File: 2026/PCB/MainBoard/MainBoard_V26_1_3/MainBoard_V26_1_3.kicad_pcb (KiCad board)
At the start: 2 copper layers, 100 x 65 mm, 94 parts, among them J1 Raspberry_Pi_2_3, J15 TFT3, J16 CAN_CON, J2 fan, J3 MOLEX, J5 Conn_01x05_Socket, J6 Debug, Q1 Q_NMOS_GSD, Q2 Q_NMOS_GSD, SW1 SW_MEC_5E, SW2 Ras_1, SW3 Ras_2, SW4 SW_Wuerth_450301014042, SW5 SW_MEC_5E, SW6 SW_MEC_5E, U1 STM32F446RETx, U10 MPU9250, U2 LMR51460FSQDRRRQ1, U3 MOUDLE-SEEEDUINO-XIAO, U5 MCP1703AT-3302E/CB, U6 BNO055, U7 LTC4451AV-TRPBF, U8 MAX3051, Y1 CSTNE16M0V530000R0

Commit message: 回路修正、PCB大枠決定
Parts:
- removed R9: 2.2k, Resistor_SMD:R_0603_1608Metric_Pad0.98x0.95mm_HandSolder
- removed SW4: SW_Wuerth_450301014042, 0_Library:slideSW
- removed SW5, SW6: SW_MEC_5E, 0_Library:SW_SKRPACE010
- removed U10: MPU9250, Connector_PinHeader_2.54mm:PinHeader_1x10_P2.54mm_Vertical
- added C26: 0.1u, Capacitor_SMD:C_0603_1608Metric_Pad1.08x0.95mm_HandSolder, F.Cu at (204.3, 33.6)
- added C27: 0.1u, Capacitor_SMD:C_0603_1608Metric_Pad1.08x0.95mm_HandSolder, F.Cu at (204.3, 36.1)
- added C28: 0.1u, Capacitor_SMD:C_0603_1608Metric_Pad1.08x0.95mm_HandSolder, F.Cu at (204.3, 38.6)
- added R1: 100k, Resistor_SMD:R_0603_1608Metric_Pad0.98x0.95mm_HandSolder, F.Cu at (204.3, 41.1)
- added U9: LTC4451AV-TRPBF, 0_Library:05-08-1683_ADI, F.Cu at (208.5, 39.7)
- R10: value 4.7k -> 100k
- R11: value 1k -> 10k
- R8: value 2.2k -> 10k
- SW1: moved to F.Cu
- U3: moved to B.Cu
- U6: value BNO055 -> LSM6DSO32XTR; footprint Connector_PinHeader_2.54mm:PinHeader_1x04_P2.54mm_Vertical -> 0_Library:LGA_O32XTR_STM-M; moved to F.Cu
- moved ROTSW1 85.8 mm to (251.6, 68.5), turned to 90 degrees
- moved G*** 78.3 mm to (138.7, 63.7)
- moved SW3 67.5 mm to (248.7, 61.2), turned to -90 degrees
- moved R8 64.3 mm to (204.3, 43.6), turned to 0 degrees
- moved U3 62.9 mm to (252.1, 124.3)
- moved SW1 61.1 mm to (232.2, 61.7), turned to 0 degrees
- moved SW2 51.1 mm to (241.2, 61.2), turned to -90 degrees
- moved U6 44.6 mm to (214.4, 84.5)
- moved G*** 15.4 mm to (188.7, 46.4)
- moved C24 5.20 mm to (188.2, 81.4), turned to 90 degrees
- moved D11 4.59 mm to (259.2, 108.0)
- moved D14 4.59 mm to (259.2, 105.0)
- moved D3 4.59 mm to (259.2, 106.5)
- moved R16 4.59 mm to (259.2, 108.0)
- moved R19 4.59 mm to (259.2, 105.0)
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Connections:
- C18 pad 1: +5V -> 5V_For3.3V
- D3 pad 2: 5V_Rock -> +5V
- J1 pad 26: unconnected-(J1-~{CE1}/GPIO7-Pad26) -> ESTOP
- R8 pad 1: I2C_SDA -> ESTOP
- U1 pad 24: SPI1.CS -> unconnected-(U1-PC4-Pad24)
- U1 pad 28: SPI2.CS -> unconnected-(U1-PB2-Pad28)
- U1 pad 33: LED1 -> SPI2.CS
- U1 pad 39: imu.reset -> unconnected-(U1-PC8-Pad39)
- U1 pad 50: unconnected-(U1-PA15-Pad50) -> SPI1.CS
- U1 pad 57: discharge -> unconnected-(U1-PB5-Pad57)
- U1 pad 58: I2C_SCL -> unconnected-(U1-PB6-Pad58)
- U1 pad 59: I2C_SDA -> unconnected-(U1-PB7-Pad59)
- U1 pad 60: Net-(SW4-B) -> unconnected-(U1-BOOT0-Pad60)
- U1 pad 61: unconnected-(U1-PB8-Pad61) -> LED1
- U1 pad 8: unconnected-(U1-PC0-Pad8) -> ESTOP
- U5 pad 3: +5V -> 5V_For3.3V
- U6 pad 1: +3.3V -> SPI1.MISO
- U6 pad 3: I2C_SDA -> GND
- U6 pad 4: I2C_SCL -> unconnected-(U6-INT1-Pad4)
- U7 pad 1: +5V -> unconnected-(U7-VCC-Pad1)
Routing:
- net +3.3V: track 314.4 -> 0.00 mm, vias 9 -> 0
- net 5V_Rock: track 131.9 -> 0.00 mm, vias 19 -> 0
- net +5V: track 113.1 -> 0.00 mm, vias 4 -> 0
- net LED_RAS2: track 113.1 -> 0.00 mm, vias 1 -> 0
- net LED_RAS1: track 110.6 -> 0.00 mm, vias 1 -> 0
- net SPI2.CS: track 94.1 -> 0.00 mm, vias 2 -> 0
- net SPI2.CLK: track 80.8 -> 0.00 mm, vias 2 -> 0
- net UI_Audio: track 78.5 -> 0.00 mm, vias 1 -> 0
- net NRST: track 69.0 -> 0.00 mm, vias 5 -> 0
- net LED_CS: track 64.6 -> 0.00 mm, vias 1 -> 0
- net SPI2.MOSI: track 63.6 -> 0.00 mm
- net SPI1.CLK: track 60.7 -> 0.00 mm, vias 1 -> 0
- net SPI2.MISO: track 60.5 -> 0.00 mm
- net BATTERY_MEASURE: track 59.5 -> 0.00 mm, vias 2 -> 0
- net MD3_TX: track 57.7 -> 0.00 mm, vias 2 -> 0
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- removed copper zone on B.Cu, net +24V
- removed copper zone on B.Cu, net Net-(C15-Pad2)
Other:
- board text removed: "BOOT-ON/OFF"
- board text removed: "Discharge"
- board text removed: "IMU"

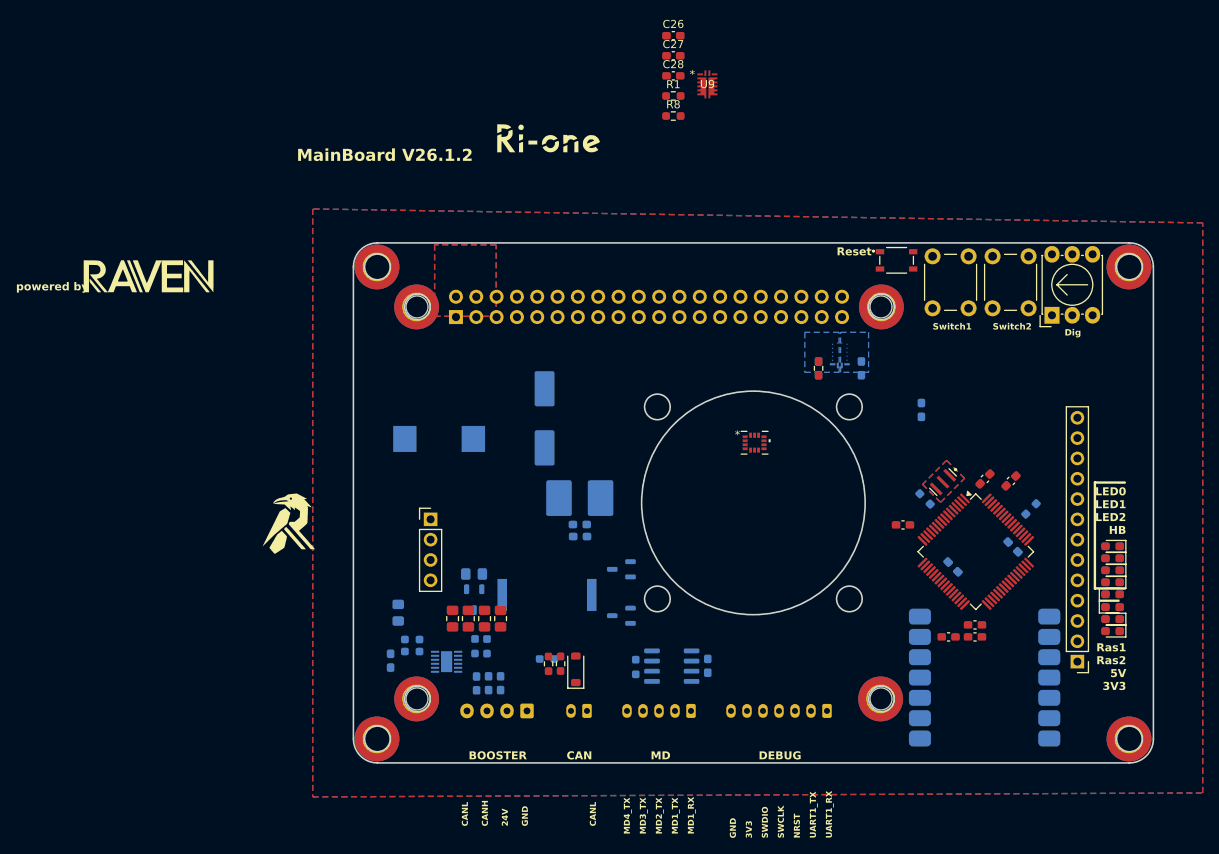
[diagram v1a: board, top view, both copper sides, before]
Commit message: 基板外形、ESTOP変更、配置決定
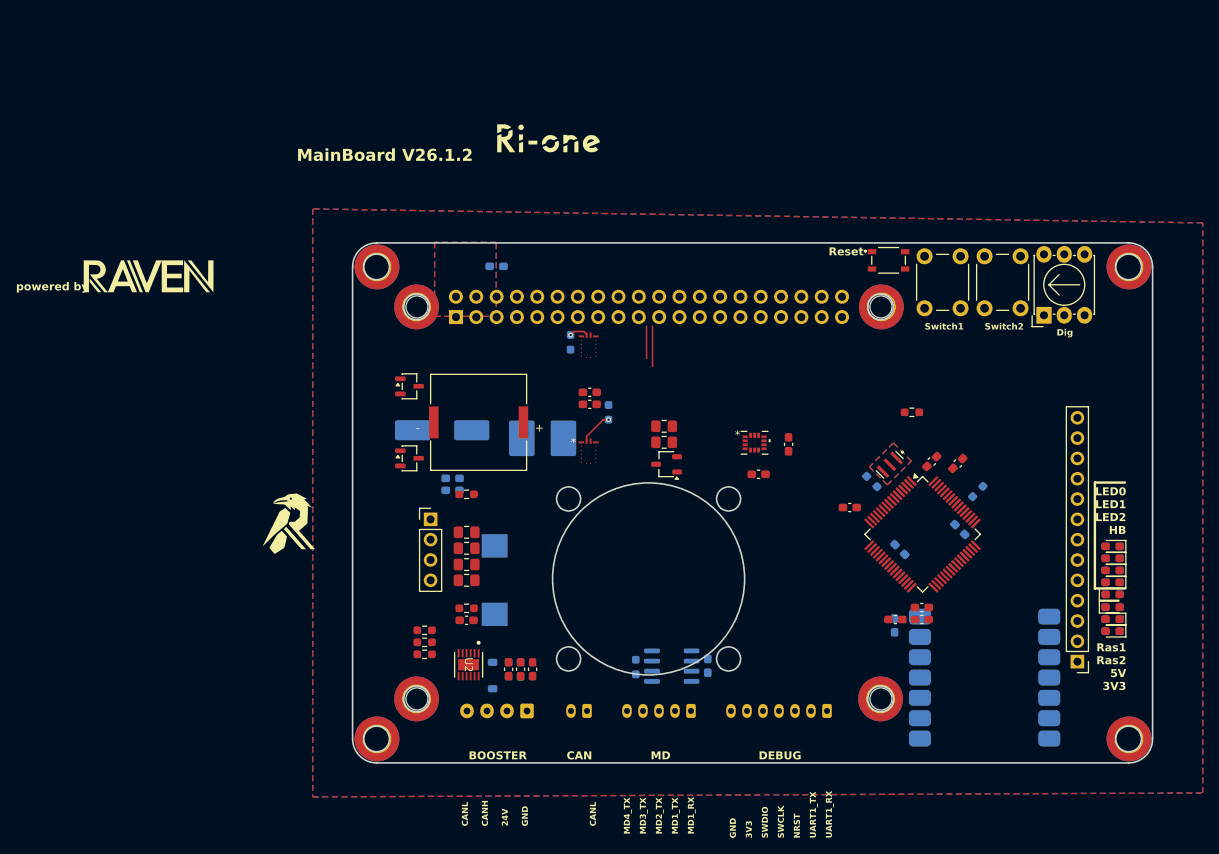
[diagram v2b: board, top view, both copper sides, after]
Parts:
- C11, C13, C15, C17, C18, C19, C25, LS1, Q1, Q2, R2, R21, R3, R4, R7, U2, U5, U7: moved to F.Cu
- D6, R1, R10, R11, R17: moved to B.Cu
- moved C27 53.4 mm to (214.9, 88.4), turned to 180 degrees
- moved U9 48.3 mm to (193.7, 85.7)
- moved C28 48.3 mm to (218.7, 84.7), turned to -90 degrees
- moved R8 47.5 mm to (234.1, 80.7)
- moved C23 47.3 mm to (182.2, 62.4), turned to 0 degrees
- moved C26 47.2 mm to (193.9, 79.7)
- moved R1 40.4 mm to (196.2, 80.7), turned to 90 degrees
- moved C18 39.5 mm to (203.1, 84.4), turned to 0 degrees
- moved Q1 35.0 mm to (171.3, 77.4), turned to 0 degrees
- moved Q2 33.0 mm to (171.3, 86.4), turned to 0 degrees
- moved U7 31.4 mm to (193.7, 72.4)
- moved R17 31.2 mm to (191.4, 71.9), turned to -90 degrees
- moved C17 30.1 mm to (203.1, 82.4), turned to 0 degrees
- moved U5 29.4 mm to (203.4, 87.2), turned to 180 degrees
- moved C25 28.8 mm to (193.9, 78.2), turned to 0 degrees
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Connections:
- J1 pad 26: ESTOP -> unconnected-(J1-~{CE1}/GPIO7-Pad26)
- J1 pad 37: unconnected-(J1-GPIO26-Pad37) -> ESTOP
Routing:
- net Net-(U9-SHDN#): track 0.00 -> 4.21 mm, vias 0 -> 1
- net Net-(U7-SHDN#): track 0.00 -> 2.47 mm, vias 0 -> 1
- removed copper zone on B.Cu, net +5V
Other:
- outline, holes or cut-outs redrawn

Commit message: 途中保存
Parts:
- R8: moved to B.Cu
- moved R5 10.2 mm to (229.7, 79.2), turned to -135 degrees
- moved R8 6.29 mm to (228.4, 77.9), turned to 45 degrees
- moved C1 6.05 mm to (232.8, 100.6)
- moved C2 6.05 mm to (237.3, 80.8)
- moved C4 6.05 mm to (236.1, 99.1)
- moved C5 6.05 mm to (240.8, 89.3)
- moved C6 6.05 mm to (240.6, 81.1)
- moved C7 6.05 mm to (227.1, 86.6)
- moved C8 6.05 mm to (236.1, 100.6)
- moved R1 6.05 mm to (243.1, 84.6)
- moved U1 6.05 mm to (236.2, 89.9)
- moved Y1 6.05 mm to (232.1, 81.2)
- moved C3 4.16 mm to (229.2, 95.4)
- moved R7 0.50 mm to (178.4, 90.4)
- moved C25 0.15 mm to (193.7, 78.2)
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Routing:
- net +3.3V: track 0.00 -> 115.9 mm, vias 0 -> 1
- net SPI2.CLK: track 0.00 -> 40.6 mm, vias 0 -> 1
- net SPI2.CS: track 0.00 -> 39.6 mm, vias 0 -> 1
- net SPI2.MOSI: track 0.00 -> 39.2 mm, vias 0 -> 1
- net SPI2.MISO: track 0.00 -> 36.5 mm, vias 0 -> 1
- net NRST: track 0.00 -> 25.9 mm, vias 0 -> 3
- net LED_CS: track 0.00 -> 25.8 mm, vias 0 -> 1
- net ESTOP: track 0.00 -> 20.9 mm, vias 0 -> 1
- net Net-(Q1-D): track 0.00 -> 17.8 mm
- net +5V: track 0.00 -> 14.9 mm, vias 0 -> 24
- net D/C: track 0.00 -> 10.8 mm
- net Net-(U2-PG): track 0.00 -> 6.44 mm
- net Net-(U2-FB): track 0.00 -> 6.07 mm
- net Net-(U1-PH0): track 0.00 -> 5.13 mm
- net Net-(U2-RT): track 0.00 -> 5.03 mm
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- added copper zone on F.Cu, net +24V
- added copper zone on B.Cu, net +5V
- added copper zone on F.Cu, net +5V
- added copper zone on F.Cu, net 5V_For3.3V
- added copper zone on B.Cu, net Net-(C15-Pad2)
- added copper zone on F.Cu, net Net-(C15-Pad2)

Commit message: 途中保存2
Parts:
- C16, R20, U3, U8: moved to F.Cu
- moved D13 80.7 mm to (188.8, 63.9)
- moved R18 80.7 mm to (188.8, 63.9)
- moved D14 77.6 mm to (193.3, 63.9)
- moved R19 77.6 mm to (193.3, 63.9)
- moved G*** 24.6 mm to (212.7, 51.7)
- moved R20 20.7 mm to (220.3, 111.9), turned to 180 degrees
- moved U3 17.8 mm to (234.3, 124.3), turned to 0 degrees
- moved U8 17.1 mm to (220.4, 107.4), turned to -90 degrees
- moved C12 15.7 mm to (247.6, 106.2), turned to 180 degrees
- moved C1 12.7 mm to (220.8, 96.4)
- moved C4 12.7 mm to (224.1, 94.9)
- moved C8 12.7 mm to (224.1, 96.4)
- moved G*** 11.2 mm to (147.9, 101.9)
- moved C16 9.70 mm to (216.9, 107.4)
- moved C27 3.75 mm to (214.9, 92.2)
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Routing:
- net UI_Audio: track 0.00 -> 103.4 mm
- net +3.3V: track 115.9 -> 18.2 mm
- net +5V: track 14.9 -> 109.1 mm, vias 24 -> 26
- net T_CS: track 0.00 -> 58.6 mm
- net LCD_LED: track 0.00 -> 50.0 mm, vias 0 -> 1
- net CANL: track 0.00 -> 47.9 mm
- net CANH: track 0.00 -> 47.2 mm
- net SWCLK: track 0.00 -> 41.8 mm
- net SWDIO: track 0.00 -> 39.5 mm
- net MISO: track 0.00 -> 36.5 mm, vias 0 -> 1
- net MOSI: track 0.00 -> 35.5 mm
- net SCK: track 0.00 -> 32.3 mm, vias 0 -> 1
- net SPI1.MOSI: track 0.00 -> 29.9 mm
- net CAN1_RX: track 0.00 -> 29.5 mm
- net SPI1.MISO: track 0.00 -> 27.1 mm
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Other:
- board text added: "MainBoard V26.1.3"
- board text added: "Ras1 Ras2"
- board text removed: "MainBoard V26.1.2"

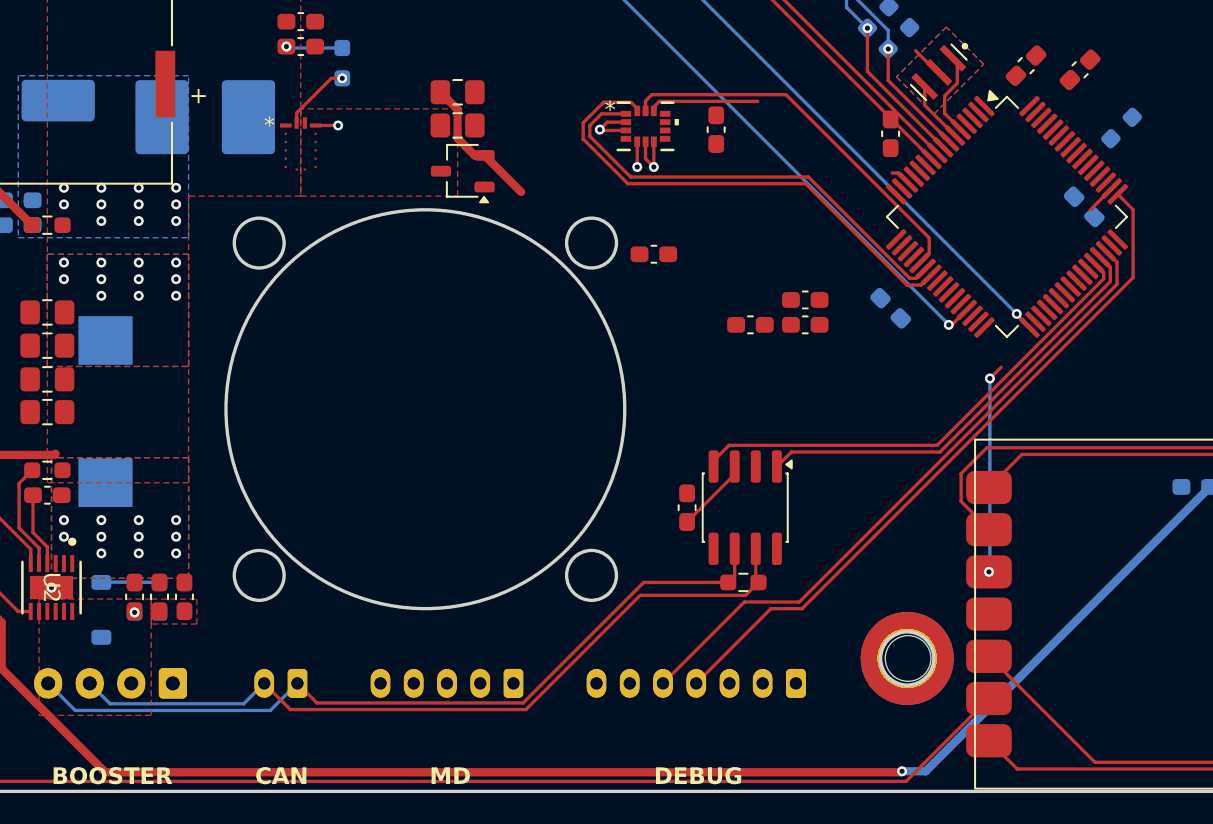
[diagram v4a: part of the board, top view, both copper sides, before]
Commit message: 途中保存3、スピーカ抵抗変更
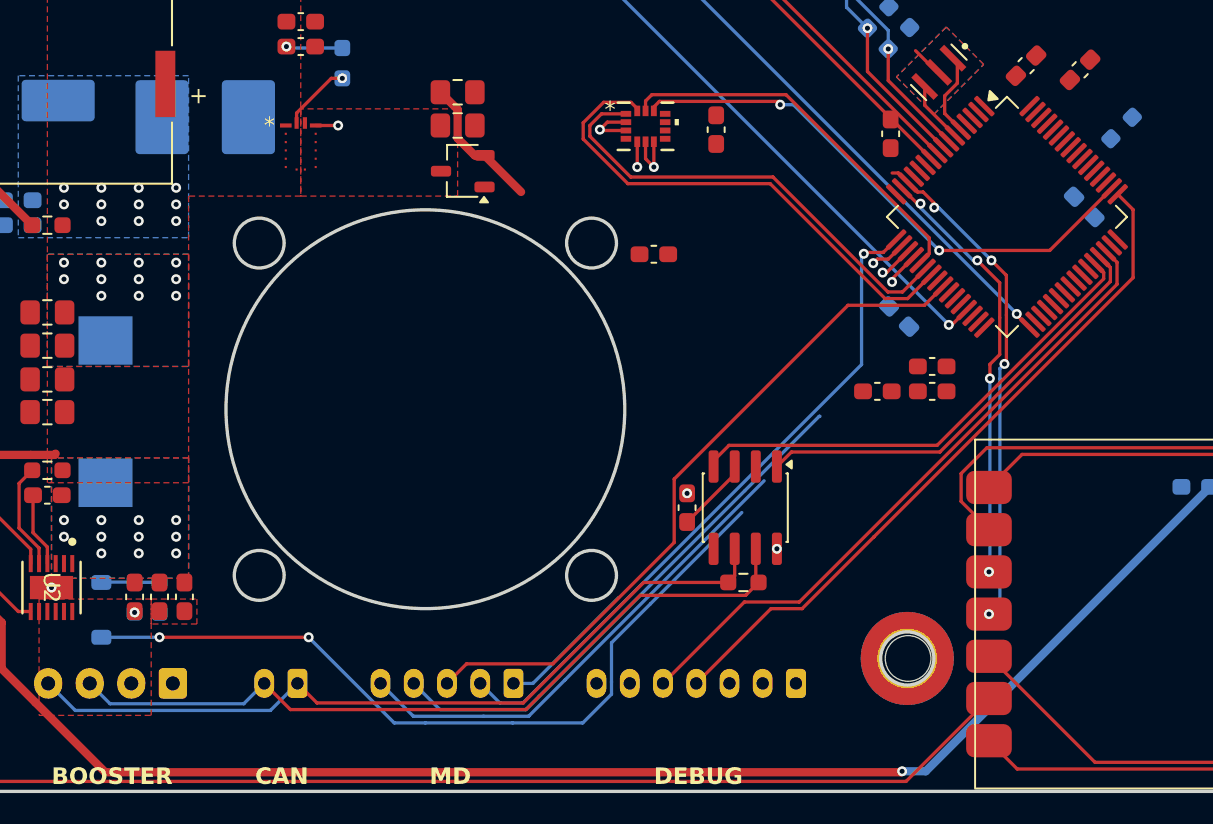
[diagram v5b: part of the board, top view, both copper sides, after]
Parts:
- R7: value 10k -> 1k
- moved C1 8.62 mm to (228.4, 100.4)
- moved C4 8.62 mm to (231.7, 98.9)
- moved C8 8.62 mm to (231.7, 100.4)
- moved C3 0.71 mm to (229.7, 95.9)
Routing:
- net BATTERY_MEASURE: track 0.00 -> 49.8 mm, vias 0 -> 3
- net MD2_TX: track 0.00 -> 42.0 mm
- net MD1_TX: track 0.00 -> 40.9 mm, vias 0 -> 1
- net MD3_TX: track 0.00 -> 32.4 mm
- net MD4_TX: track 0.00 -> 29.8 mm
- net UART4_TX: track 1.19 -> 30.4 mm, vias 0 -> 4
- net SPI1.CS: track 8.44 -> 33.3 mm, vias 0 -> 2
- net UART4_RX: track 12.6 -> 26.0 mm, vias 2 -> 4
- net MD1_RX: track 0.00 -> 8.49 mm
- net GND: track 15.1 -> 17.3 mm, vias 10 -> 13
- net +3.3V: track 18.2 -> 20.2 mm, vias 1 -> 2
- net SPI1.MOSI: track 29.9 -> 30.6 mm
- net SPI1.MISO: track 27.1 -> 27.8 mm

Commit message: 途中保存4
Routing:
- net R1: track 0.00 -> 69.3 mm, vias 0 -> 1
- net R2: track 0.00 -> 65.4 mm
- net SW_RAS2: track 0.00 -> 53.7 mm
- net R4: track 0.00 -> 51.9 mm
- net R3: track 0.00 -> 43.2 mm, vias 0 -> 1
- net SW_RAS1: track 0.00 -> 41.2 mm
- net NRST: track 30.1 -> 71.2 mm
- net UART1_RX: track 0.00 -> 38.5 mm, vias 0 -> 1
- net UART1_TX: track 0.00 -> 33.8 mm, vias 0 -> 1
- net GND: track 17.3 -> 21.4 mm, vias 13 -> 11

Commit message: 途中保存5
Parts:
- removed the R1 at (243.1, 84.6)
- C12, R5, R8: moved to F.Cu
- U3: moved to B.Cu
- moved U3 17.8 mm to (252.1, 124.3), turned to 180 degrees
- moved C12 17.5 mm to (230.7, 110.9), turned to -90 degrees
- moved C7 2.92 mm to (226.7, 83.4)
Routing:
- net NRST: track 71.2 -> 137.5 mm, vias 3 -> 5
- net MD1_RX: track 8.49 -> 40.1 mm, vias 0 -> 3
- net T_CS: track 58.6 -> 33.1 mm
- net LCD_LED: track 50.0 -> 29.8 mm
- net MD4_TX: track 29.8 -> 48.3 mm
- net D/C: track 27.0 -> 10.8 mm
- net Reset: track 20.5 -> 4.34 mm
- net UI_Audio: track 103.4 -> 119.5 mm, vias 0 -> 1
- net +5V: track 109.1 -> 94.5 mm, vias 26 -> 25
- net SCK: track 32.3 -> 46.8 mm
- net MD3_TX: track 32.4 -> 45.6 mm
- net MOSI: track 35.5 -> 47.4 mm, vias 0 -> 1
- net LED_CS: track 16.1 -> 25.8 mm
- net MISO: track 36.5 -> 45.1 mm
- net UART1_RX: track 38.5 -> 30.7 mm, vias 1 -> 0
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
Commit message: 途中保存6
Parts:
- C8: moved to B.Cu
- moved C6 3.12 mm to (237.9, 79.4)
- moved C5 3.00 mm to (238.2, 87.9)
- moved C1 2.86 mm to (230.4, 98.4), turned to -135 degrees
- moved C27 2.75 mm to (214.9, 89.4)
- moved C2 2.75 mm to (236.7, 78.2)
- moved C3 2.61 mm to (230.4, 98.4), turned to 45 degrees
- moved C7 1.80 mm to (227.8, 84.8), turned to -45 degrees
- moved C4 0.75 mm to (231.7, 99.7), turned to 45 degrees
- moved C8 0.75 mm to (231.7, 99.7), turned to -135 degrees
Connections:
- U1 pad 34: LED2 -> unconnected-(U1-PB13-Pad34)
- U1 pad 35: LED3 -> unconnected-(U1-PB14-Pad35)
- U1 pad 36: LED4 -> unconnected-(U1-PB15-Pad36)
- U1 pad 41: HEART_BEAT_LED -> unconnected-(U1-PA8-Pad41)
- U1 pad 55: unconnected-(U1-PB3-Pad55) -> HEART_BEAT_LED
- U1 pad 57: unconnected-(U1-PB5-Pad57) -> LED2
- U1 pad 58: unconnected-(U1-PB6-Pad58) -> LED3
- U1 pad 59: unconnected-(U1-PB7-Pad59) -> LED4
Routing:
- net +3.3V: track 16.5 -> 179.3 mm, vias 2 -> 15
- net MD3_TX: track 45.6 -> 77.7 mm, vias 0 -> 1
- net MD4_TX: track 48.3 -> 62.9 mm, vias 0 -> 1
- net UART1_RX: track 30.7 -> 38.5 mm, vias 0 -> 1
- net UART1_TX: track 26.8 -> 34.2 mm, vias 0 -> 1
- net BATTERY_MEASURE: track 56.1 -> 61.0 mm, vias 3 -> 5
- net Net-(U1-VCAP_1): track 0.00 -> 3.87 mm
- net SPI2.CS: track 37.9 -> 39.7 mm
- net GND: track 28.1 -> 29.7 mm, vias 12 -> 19
